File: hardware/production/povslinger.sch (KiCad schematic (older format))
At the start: 45 parts, among them J1 DEBUG, Q1 BSS138, Q2 BSS138, U1 LF33_TO252, U2 L7805, U3 ESP-12E, U4 US5881 or similar, U5 LIS2HH12

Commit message: Update some resistor values, remove backup schematics
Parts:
- C1, C2: value 330n -> 4.7u
- C3, C6: value 10u -> 22u
- C4: value 10u -> 4.7u
- C5: value 10n -> 100n
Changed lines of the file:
@@
 P 4500 7350
 F 0 "C1" H 4510 7420 50  0000 L CNN
-F 1 "330n" H 4510 7270 50  0000 L CNN
+F 1 "4.7u" H 4510 7270 50  0000 L CNN
 F 2 "Capacitors_SMD:C_0603" H 4500 7350 50  0001 C CNN
 F 3 "" H 4500 7350 50  0001 C CNN
@@
 P 5400 7350
 F 0 "C4" H 5410 7420 50  0000 L CNN
-F 1 "10u" H 5410 7270 50  0000 L CNN
+F 1 "4.7u" H 5410 7270 50  0000 L CNN
 F 2 "Capacitors_SMD:C_0603" H 5400 7350 50  0001 C CNN
 F 3 "" H 5400 7350 50  0001 C CNN
@@
 P 4550 6400
 F 0 "C2" H 4560 6470 50  0000 L CNN
-F 1 "330n" H 4560 6320 50  0000 L CNN
+F 1 "4.7u" H 4560 6320 50  0000 L CNN
 F 2 "Capacitors_SMD:C_0603" H 4550 6400 50  0001 C CNN
 F 3 "" H 4550 6400 50  0001 C CNN
@@
 P 5350 6400
 F 0 "C3" H 5360 6470 50  0000 L CNN
-F 1 "10u" H 5360 6320 50  0000 L CNN
+F 1 "22u" H 5360 6320 50  0000 L CNN
 F 2 "Capacitors_SMD:C_0603" H 5350 6400 50  0001 C CNN
 F 3 "" H 5350 6400 50  0001 C CNN
@@
 P 9500 3800
 F 0 "C6" H 9510 3870 50  0000 L CNN
-F 1 "10u" H 9510 3720 50  0000 L CNN
+F 1 "22u" H 9510 3720 50  0000 L CNN
 F 2 "Capacitors_SMD:C_0603" H 9500 3800 50  0001 C CNN
 F 3 "" H 9500 3800 50  0001 C CNN
@@
 P 9300 3800
 F 0 "C5" H 9310 3870 50  0000 L CNN
-F 1 "10n" H 9310 3720 50  0000 L CNN
+F 1 "100n" H 9310 3720 50  0000 L CNN
 F 2 "Capacitors_SMD:C_0603" H 9300 3800 50  0001 C CNN
 F 3 "" H 9300 3800 50  0001 C CNN

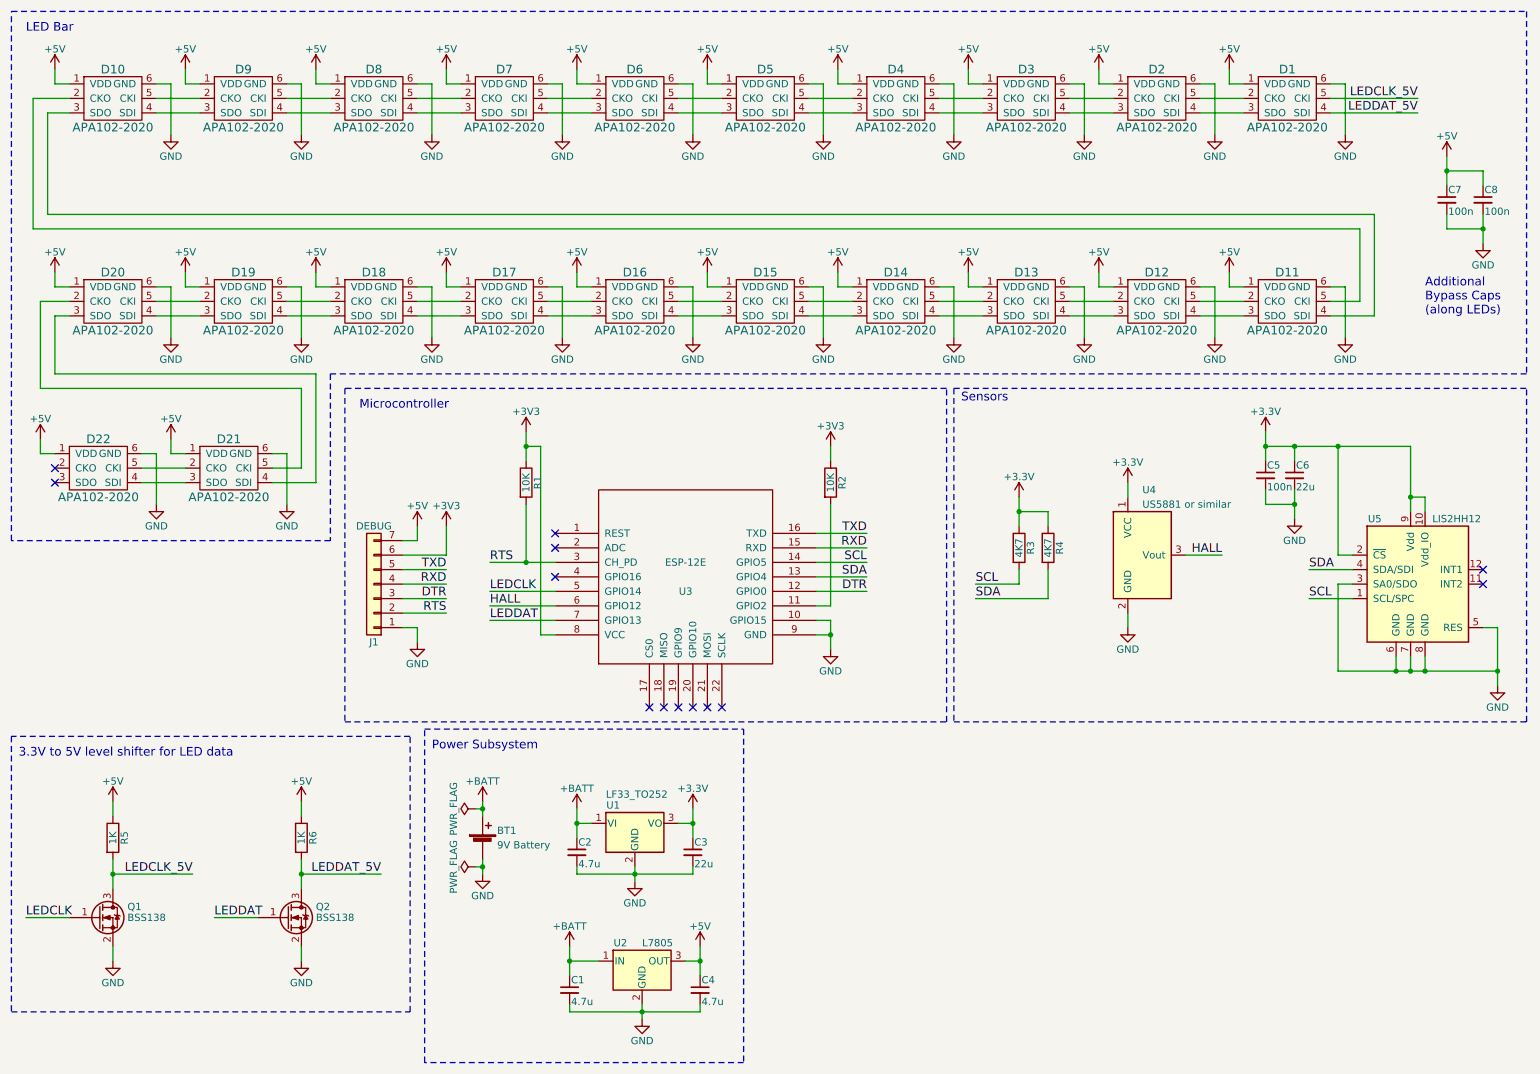
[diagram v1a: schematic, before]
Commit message: Firmware: Add pixel art function
Production Schematic: Minor layout improvements
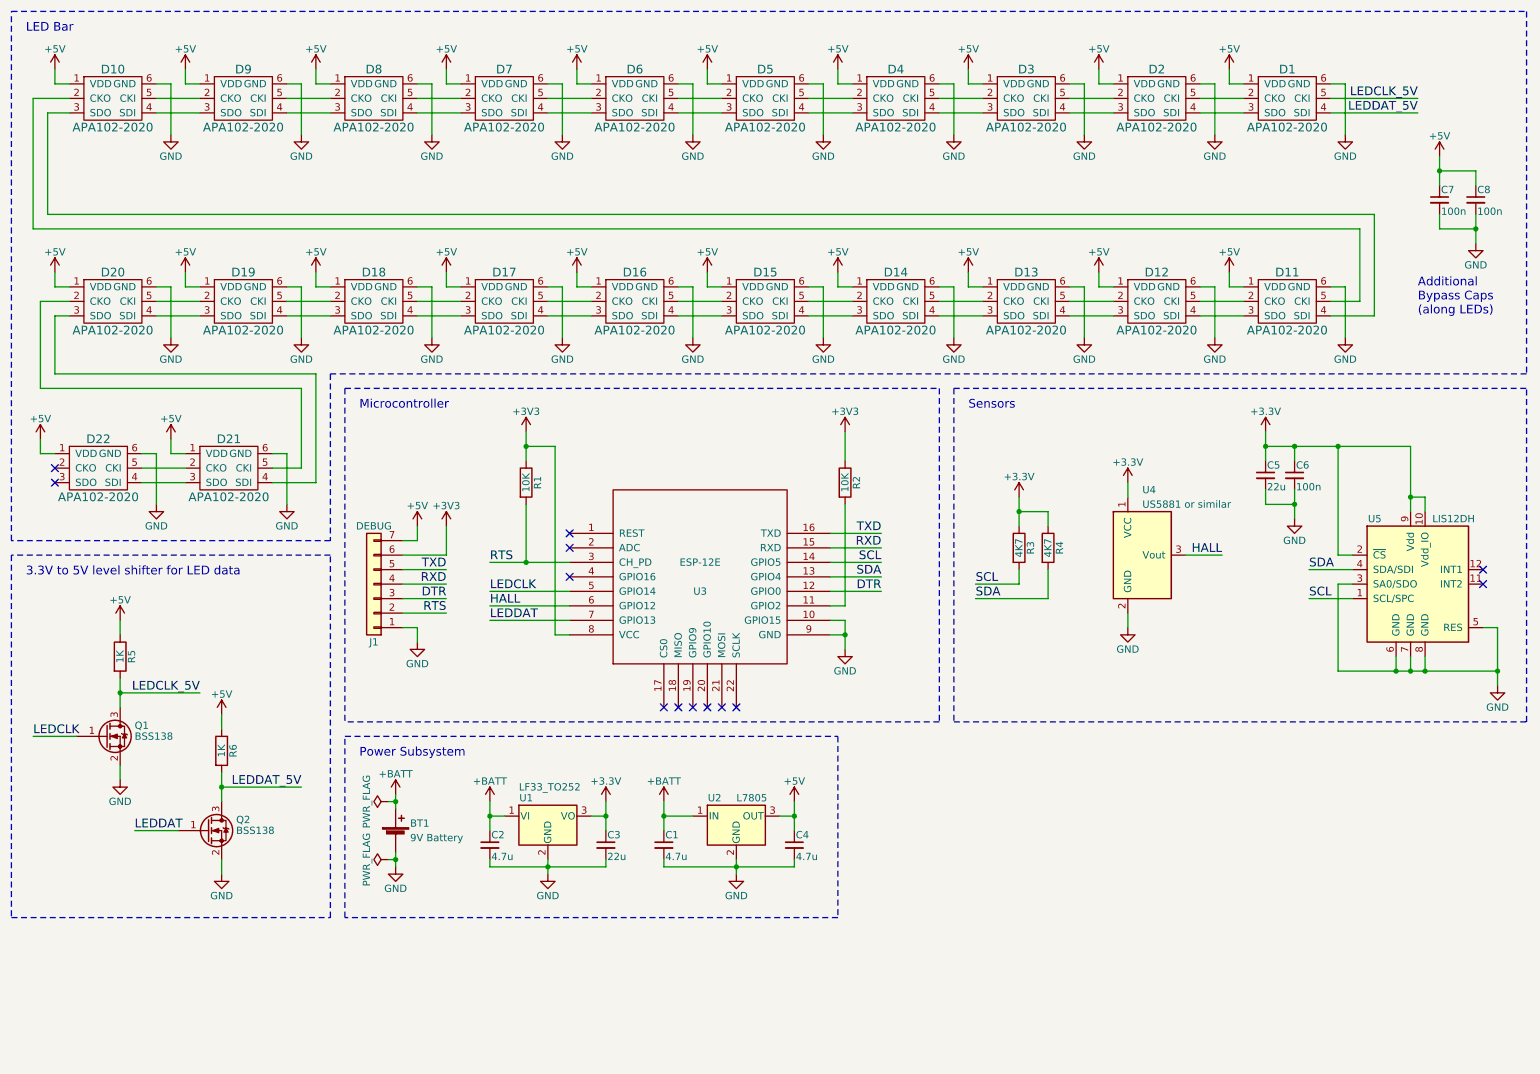
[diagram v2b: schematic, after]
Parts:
- C5: value 100n -> 22u
- C6: value 22u -> 100n
- U5: value LIS2HH12 -> LIS12DH
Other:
- moved on the sheet: BT1, C1, C2, C3, C4, C7, C8, Q1, Q2, R2, R5, R6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
